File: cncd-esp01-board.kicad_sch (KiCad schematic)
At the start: 23 parts, among them J1 ESP, J2 CTRL, SW1 RESET, U1 TL431DBZ, U2 AMS1117-3.3, U3 SN74AHC1G04DBVR, U4 SN74LVC1G126DBVR, U5 SN74LVC1G126DBVR, U6 SN74LVC1T45DBVR

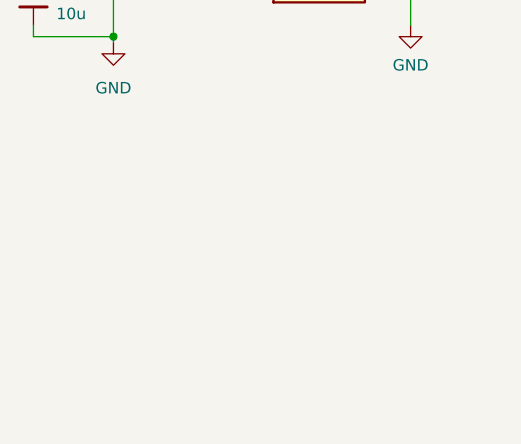
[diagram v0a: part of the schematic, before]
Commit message: Add 100uF bypass capacitor to mitigate #1
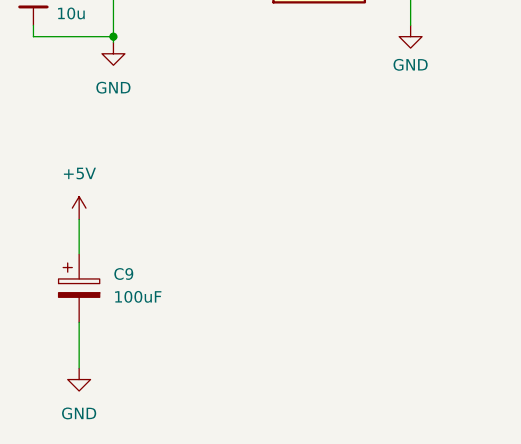
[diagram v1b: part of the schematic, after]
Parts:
- added C9: 100uF, Capacitor_Tantalum_SMD:CP_EIA-3528-21_Kemet-B, symbol Device:C_Polarized
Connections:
- net +5V: now also C9.1
- net GND: now also C9.2
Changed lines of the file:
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@@
+    (stroke (width 0) (type default))
+  )
+  (wire (pts (xy 22.86 113.665) (xy 22.86 118.745))
     (stroke (width 0) (type default))
   )
@@
   )
   (wire (pts (xy 274.32 36.195) (xy 274.32 40.64))
+    (stroke (width 0) (type default))
+  )
+  (wire (pts (xy 22.86 102.235) (xy 22.86 106.045))
     (stroke (width 0) (type default))
   )
@@
     )
   )
+  (symbol (lib_id "Device:C_Polarized") (at 22.86 109.855 0) (unit 1)
+    (in_bom yes) (on_board yes) (dnp no) (fields_autoplaced)
+    (property "Reference" "C9" (at 26.67 108.331 0)
+      (effects (font (size 1.27 1.27)) (justify left))
+    )
+    (property "Value" "100uF" (at 26.67 110.871 0)
+      (effects (font (size 1.27 1.27)) (justify left))
+    )
+    (property "Footprint" "Capacitor_Tantalum_SMD:CP_EIA-3528-21_Kemet-B" (at 23.8252 113.665 0)
+      (effects (font (size 1.27 1.27)) hide)
+    )
+    (property "Datasheet" "~" (at 22.86 109.855 0)
+      (effects (font (size 1.27 1.27)) hide)
+    )
+    (pin "1")
+    (pin "2")
+    (instances
+      (project "cncd-esp01-board"
+        (path "/e57c4501-0620-42ab-bb8f-bafe820a366a"
+          (reference "C9") (unit 1)
+        )
+      )
+    )
+  )
   (symbol (lib_id "Device:C_Small") (at 92.71 86.36 0) (unit 1)
     (in_bom yes) (on_board yes) (dnp no) (fields_autoplaced)
@@
     )
   )
+  (symbol (lib_id "power:GND") (at 22.86 118.745 0) (unit 1)
+    (in_bom yes) (on_board yes) (dnp no) (fields_autoplaced)
+    (property "Reference" "#PWR023" (at 22.86 125.095 0)
+      (effects (font (size 1.27 1.27)) hide)
+    )
+    (property "Value" "GND" (at 22.86 123.825 0)
+      (effects (font (size 1.27 1.27)))
+    )
+    (property "Footprint" "" (at 22.86 118.745 0)
+      (effects (font (size 1.27 1.27)) hide)
+    )
+    (property "Datasheet" "" (at 22.86 118.745 0)
+      (effects (font (size 1.27 1.27)) hide)
+    )
+    (pin "1")
+    (instances
+      (project "cncd-esp01-board"
+        (path "/e57c4501-0620-42ab-bb8f-bafe820a366a"
+          (reference "#PWR023") (unit 1)
+        )
+      )
+    )
+  )
   (symbol (lib_id "power:GND") (at 26.67 82.55 0) (unit 1)
     (in_bom yes) (on_board yes) (dnp no) (fields_autoplaced)
@@
         )
       )
+    )
+  )
+  (symbol (lib_id "power:+5V") (at 22.86 102.235 0) (unit 1)
+    (in_bom yes) (on_board yes) (dnp no) (fields_autoplaced)
+    (property "Reference" "#PWR022" (at 22.86 106.045 0)
+      (effects (font (size 1.27 1.27)) hide)
+    )
+    (property "Value" "+5V" (at 22.86 97.155 0)
+      (effects (font (size 1.27 1.27)))
+    )
+    (property "Footprint" "" (at 22.86 102.235 0)
+      (effects (font (size 1.27 1.27)) hide)
+    )
+    (property "Datasheet" "" (at 22.86 102.235 0)
+      (effects (font (size 1.27 1.27)) hide)
+    )
+    (pin "1")
+    (instances
+      (project "cncd-esp01-board"
+        (path "/e57c4501-0620-42ab-bb8f-bafe820a366a"
+          (reference "#PWR022") (unit 1)
+        )
+      )
